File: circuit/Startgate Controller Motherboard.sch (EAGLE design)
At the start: 11 parts, among them IC1 MAX3490ESA, IC2 L293D, U1 PROMINI, U2 TCA9548A, X1 RJ45-8L21-B, X2 SOLENOID

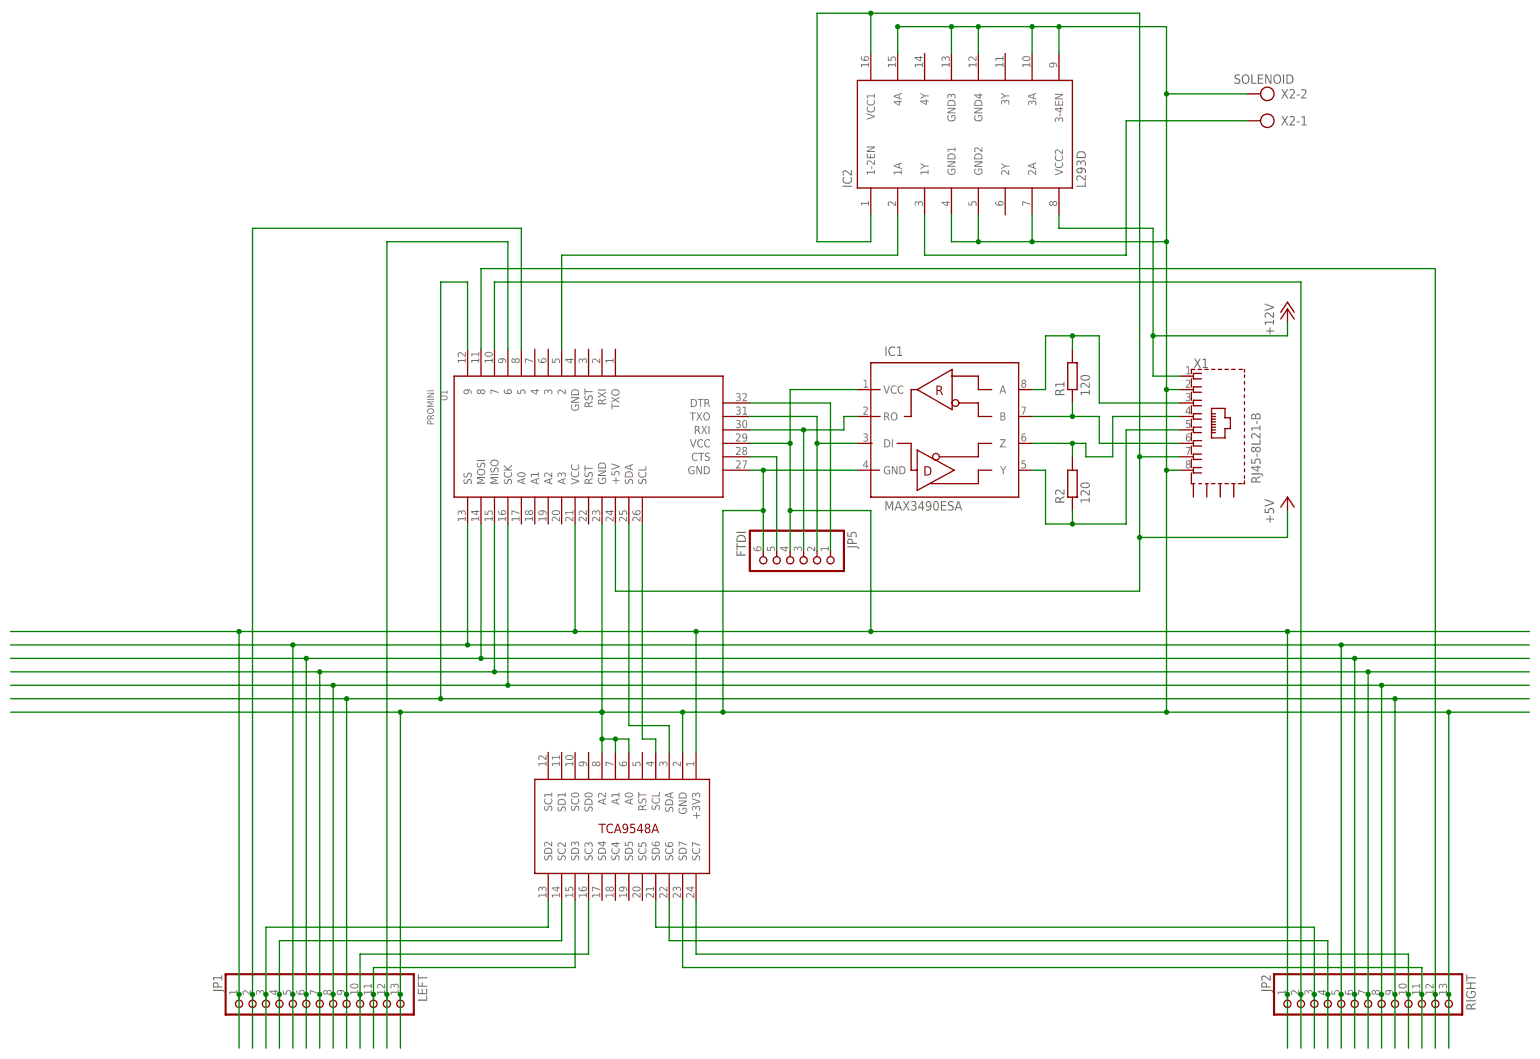
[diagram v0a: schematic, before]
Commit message: create the final schematics and boards
Some schematics errors have been corrected. Another connector for
the laser diodes of the Finishing Gate has been added. The
connectors to the daughterboards have been rotated, so that the
cabling will run mostly straight.

All gerber files have been added as well as .zip files for the
boardhouse.
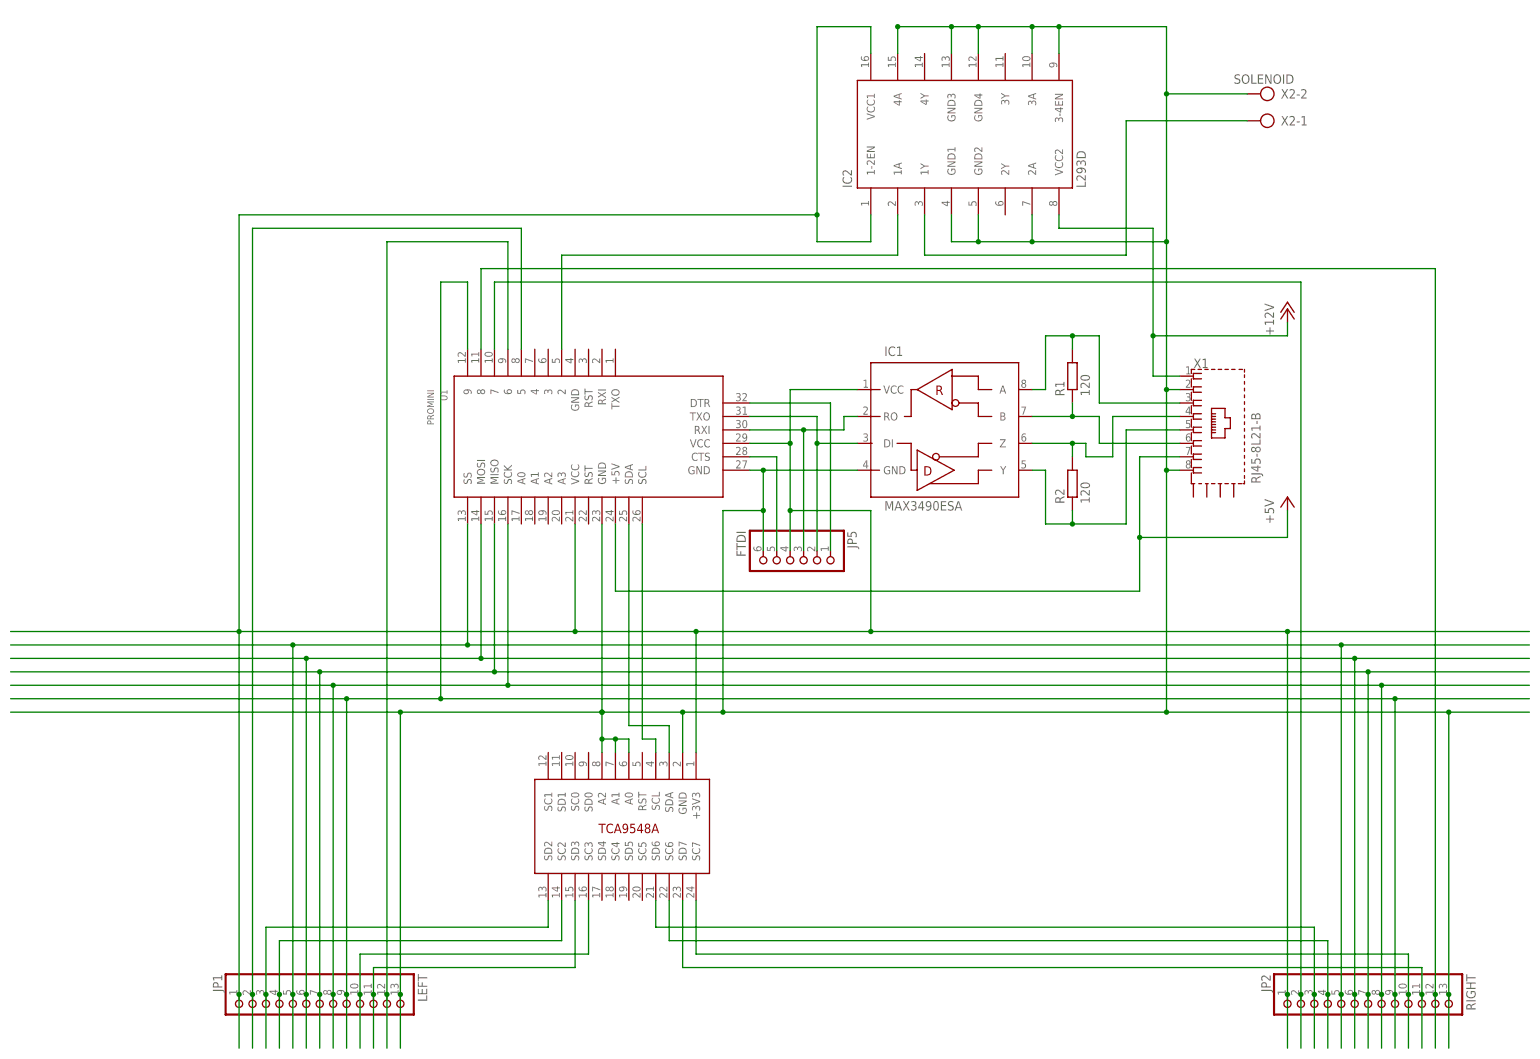
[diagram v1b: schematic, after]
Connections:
- net +3V3: now also IC2.1-2EN, IC2.VCC1
- net +5V: no longer IC2.1-2EN, IC2.VCC1
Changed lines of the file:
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@@
 <junction x="144.78" y="129.54"/>
 <junction x="160.02" y="106.68"/>
+<pinref part="IC2" gate="G$1" pin="VCC1"/>
+<wire x1="160.02" y1="220.98" x2="160.02" y2="215.9" width="0.1524" layer="91"/>
+<wire x1="149.86" y1="220.98" x2="160.02" y2="220.98" width="0.1524" layer="91"/>
+<pinref part="IC2" gate="G$1" pin="1-2EN"/>
+<wire x1="160.02" y1="185.42" x2="160.02" y2="180.34" width="0.1524" layer="91"/>
+<wire x1="160.02" y1="180.34" x2="149.86" y2="180.34" width="0.1524" layer="91"/>
+<wire x1="149.86" y1="180.34" x2="149.86" y2="185.42" width="0.1524" layer="91"/>
+<wire x1="149.86" y1="185.42" x2="149.86" y2="220.98" width="0.1524" layer="91"/>
+<wire x1="40.64" y1="106.68" x2="40.64" y2="185.42" width="0.1524" layer="91"/>
+<wire x1="40.64" y1="185.42" x2="149.86" y2="185.42" width="0.1524" layer="91"/>
+<junction x="149.86" y="185.42"/>
 </segment>
 </net>
@@
 <wire x1="210.82" y1="114.3" x2="111.76" y2="114.3" width="0.1524" layer="91"/>
 <wire x1="111.76" y1="114.3" x2="111.76" y2="127" width="0.1524" layer="91"/>
-<wire x1="210.82" y1="139.7" x2="210.82" y2="223.52" width="0.1524" layer="91"/>
-<pinref part="IC2" gate="G$1" pin="VCC1"/>
-<wire x1="210.82" y1="223.52" x2="160.02" y2="223.52" width="0.1524" layer="91"/>
-<wire x1="160.02" y1="223.52" x2="160.02" y2="215.9" width="0.1524" layer="91"/>
-<junction x="210.82" y="139.7"/>
 <wire x1="238.76" y1="124.46" x2="210.82" y2="124.46" width="0.1524" layer="91"/>
 <junction x="210.82" y="124.46"/>
-<pinref part="IC2" gate="G$1" pin="1-2EN"/>
-<wire x1="160.02" y1="185.42" x2="160.02" y2="180.34" width="0.1524" layer="91"/>
-<wire x1="160.02" y1="180.34" x2="149.86" y2="180.34" width="0.1524" layer="91"/>
-<wire x1="149.86" y1="180.34" x2="149.86" y2="223.52" width="0.1524" layer="91"/>
-<wire x1="149.86" y1="223.52" x2="160.02" y2="223.52" width="0.1524" layer="91"/>
-<junction x="160.02" y="223.52"/>
-</segment>
-</net>
+</segment>
+</net>
